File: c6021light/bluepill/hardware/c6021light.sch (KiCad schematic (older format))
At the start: 77 parts, among them J1 Barrel_Jack_Switch, J10 Conn_01x02, J11 Conn_01x02, J12 XpressNet, J2 Conn_02x04_Odd_Even, J3 Conn_02x16_Row_Letter_First, J30 Loconet, J31 Conn_01x02, J32 Conn_01x02, J4 Conn_01x02, J5 Grove I2C, J50 USB_B_Micro, J51 Conn_01x06, J52 Debug UART, J6 Conn_01x02, J7 Conn_01x02, J8 RJ45, Q30 BC337, Q31 BC547, Q32 BC547, SW1 SW_Push, U1 L7805, U10 SN75176, U2 L7808, U3 MCP2562, U30 LM393, U4 ISO1050DUB, U50 CH340C

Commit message: work on new revision
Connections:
- net +12V: no longer TP1.1 (Pin_1), TP2.1 (Pin_1)
- net GNDD: no longer J8.5
- no-connect marks 24 -> 28
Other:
- moved on the sheet: TP1, TP2
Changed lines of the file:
@@
 Sheet 1 1
 Title "C6021 Light"
-Date "2020-06-09"
-Rev "1.0"
+Date "2020-08-03"
+Rev "1.1"
 Comp "Damian Philipp / Gerhard Bertelsmann"
 Comment1 ""
@@
 	7725 900  7725 1000
 $Comp
-L Connector:RJ45 J8
-U 1 1 5EDB2E8F
-P 9575 1200
-F 0 "J8" H 9245 1204 50  0000 R CNN
-F 1 "RJ45" H 9245 1295 50  0000 R CNN
-F 2 "w_conn_pc:mebp8" V 9575 1225 50  0001 C CNN
-F 3 "~" V 9575 1225 50  0001 C CNN
-	1    9575 1200
-	-1   0    0    1
-$EndComp
-$Comp
 L Device:C C5
 U 1 1 5EDB8D27
@@
 Wire Wire Line
 	9175 1200 9025 1200
-Wire Wire Line
-	9175 1300 9025 1300
 Wire Wire Line
 	9175 1400 8925 1400
@@
 	8925 1400 8925 1000
 Wire Wire Line
-	9025 1300 9025 1900
-Wire Wire Line
 	8325 1500 9175 1500
-Wire Wire Line
-	9025 1300 9025 1200
-Connection ~ 9025 1300
 Wire Notes Line
 	6975 2025 11200 2025
@@
 	1150 1425 1200 1425
 Wire Wire Line
-	1200 1425 1200 2050
-Wire Wire Line
 	1200 2400 1500 2400
 Connection ~ 1200 1425
@@
 Connection ~ 5850 4225
 $Comp
-L Connector_Generic:Conn_01x01 TP1
-U 1 1 5EE1214D
-P 1000 2050
-F 0 "TP1" H 918 1917 50  0000 C CNN
-F 1 "Conn_01x01" H 918 1916 50  0001 C CNN
-F 2 "TestPoint:Test_Point_NA" H 1000 2050 50  0001 C CNN
-F 3 "~" H 1000 2050 50  0001 C CNN
-	1    1000 2050
-	-1   0    0    1
-$EndComp
-Connection ~ 1200 2050
-Wire Wire Line
-	1200 2050 1200 2300
-$Comp
 L Connector_Generic:Conn_01x01 TP2
 U 1 1 5EE12B1B
-P 1000 2300
-F 0 "TP2" H 918 2167 50  0000 C CNN
-F 1 "Conn_01x01" H 918 2166 50  0001 C CNN
-F 2 "TestPoint:Test_Point_NA" H 1000 2300 50  0001 C CNN
-F 3 "~" H 1000 2300 50  0001 C CNN
-	1    1000 2300
+P 775 2300
+F 0 "TP2" H 693 2167 50  0000 C CNN
+F 1 "Conn_01x01" H 693 2166 50  0001 C CNN
+F 2 "TestPoint:Test_Point_NA" H 775 2300 50  0001 C CNN
+F 3 "~" H 775 2300 50  0001 C CNN
+	1    775  2300
 	-1   0    0    1
 $EndComp
-Connection ~ 1200 2300
-Wire Wire Line
-	1200 2300 1200 2400
 $Comp
 L Connector_Generic:Conn_02x04_Odd_Even J2
@@
 	10375 4775 10375 5025
 Connection ~ 10375 5025
+$Comp
+L Connector:RJ45 J8
+U 1 1 5EDB2E8F
+P 9575 1200
+F 0 "J8" H 9245 1204 50  0000 R CNN
+F 1 "RJ45" H 9245 1295 50  0000 R CNN
+F 2 "w_conn_pc:mebp8" V 9575 1225 50  0001 C CNN
+F 3 "~" V 9575 1225 50  0001 C CNN
+	1    9575 1200
+	-1   0    0    1
+$EndComp
+Wire Wire Line
+	9025 1200 9025 1900
+NoConn ~ 9175 1300
+NoConn ~ 10250 8475
+$Comp
+L Connector_Generic:Conn_01x01 TP1
+U 1 1 5EE1214D
+P 775 2050
+F 0 "TP1" H 693 1917 50  0000 C CNN
+F 1 "Conn_01x01" H 693 1916 50  0001 C CNN
+F 2 "TestPoint:Test_Point_NA" H 775 2050 50  0001 C CNN
+F 3 "~" H 775 2050 50  0001 C CNN
+	1    775  2050
+	-1   0    0    1
+$EndComp
+NoConn ~ 975  2050
+Wire Wire Line
+	1200 1425 1200 2400
+NoConn ~ 975  2300
 $EndSCHEMATC

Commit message: fix some bugs on PCb
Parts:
- removed R50, R51: 0, Resistor_SMD:R_1206_3216Metric_Pad1.42x1.75mm_HandSolder, symbol Device:R
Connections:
- net CTS: now also J52.1 (Pin_1); no longer J52.5 (Pin_5)
- net DTR: no longer J52.1 (Pin_1)
- net GND: now also J50.6 (Shield)
- net RTS: now reaches J51.6 (Pin_6), U50.14 (~RTS)
- net RTS: now also J52.5 (Pin_5)
- net at C50.1, C51.1, U50.16 (VCC): now also J50.1 (VBUS)
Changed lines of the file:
@@
 Wire Wire Line
 	8175 5700 8175 5750
-$Comp
-L Device:R R50
-U 1 1 60480953
-P 4000 7200
-F 0 "R50" V 3900 7175 50  0000 L CNN
-F 1 "0" V 4000 7175 50  0000 L CNN
-F 2 "Resistor_SMD:R_1206_3216Metric_Pad1.42x1.75mm_HandSolder" V 3930 7200 50  0001 C CNN
-F 3 "~" H 4000 7200 50  0001 C CNN
-	1    4000 7200
-	1    0    0    -1
-$EndComp
 Wire Wire Line
 	4000 7350 4100 7350
@@
 Wire Wire Line
 	4100 7350 4100 7400
-Wire Wire Line
-	4000 7000 4000 7050
 $Comp
 L Device:C C51
@@
 Wire Wire Line
 	4625 5800 4625 5700
-Wire Wire Line
-	5300 5700 5300 5950
 Connection ~ 4625 5800
 Wire Wire Line
@@
 Wire Wire Line
 	5200 6100 5200 5800
-$Comp
-L Device:R R51
-U 1 1 6058F371
-P 4225 6000
-F 0 "R51" V 4125 5975 50  0000 L CNN
-F 1 "0" V 4225 5975 50  0000 L CNN
-F 2 "Resistor_SMD:R_1206_3216Metric_Pad1.42x1.75mm_HandSolder" V 4155 6000 50  0001 C CNN
-F 3 "~" H 4225 6000 50  0001 C CNN
-	1    4225 6000
-	1    0    0    -1
-$EndComp
-Wire Wire Line
-	4225 5850 4225 5700
 Wire Wire Line
 	4225 5700 4625 5700
@@
 Wire Wire Line
 	6475 6275 6275 6275
-Text Label 6275 6275 0    50   ~ 0
-DTR
 Wire Wire Line
 	6475 6675 6275 6675
-Text Label 6275 6675 0    50   ~ 0
-CTS
 NoConn ~ 6475 6575
 Wire Notes Line
@@
 Text Notes 8950 2400 0    50   ~ 0
 optional\ngalvanische Trennung CAN
-Wire Wire Line
-	4225 6150 4225 6175
 Wire Wire Line
 	4225 6175 4400 6175
@@
 	1    0    0    -1
 $EndComp
-$Comp
-L power:PWR_FLAG #FLG0103
-U 1 1 60D33B68
-P 5500 5875
-F 0 "#FLG0103" H 5500 5950 50  0001 C CNN
-F 1 "PWR_FLAG" H 5500 6048 50  0000 C CNN
-F 2 "" H 5500 5875 50  0001 C CNN
-F 3 "~" H 5500 5875 50  0001 C CNN
-	1    5500 5875
-	1    0    0    -1
-$EndComp
-Wire Wire Line
-	5300 5950 5500 5950
-Wire Wire Line
-	5500 5950 5500 5875
-Connection ~ 5300 5950
-Wire Wire Line
-	5300 5950 5300 6100
 $Comp
 L Connector_Generic:Conn_01x04 J5
@@
 	1200 1425 1200 2400
 NoConn ~ 975  2300
+Wire Wire Line
+	4000 7000 4000 7350
+Wire Wire Line
+	4225 5700 4225 6175
+Wire Wire Line
+	5300 5700 5300 6100
+Text Label 5750 7100 0    50   ~ 0
+RTS
+Text Label 6275 6675 0    50   ~ 0
+RTS
+Text Label 6275 6275 0    50   ~ 0
+CTS
 $EndSCHEMATC

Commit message: remove C32
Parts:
- removed C32: 1n, Capacitor_THT:C_Disc_D3.0mm_W1.6mm_P2.50mm, symbol Device:C
- J50: symbol Connector:USB_B_Micro -> c6021light-rescue:USB_B_Micro-Connector
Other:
- moved on the sheet: R40
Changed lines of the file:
@@
 Sheet 1 1
 Title "C6021 Light"
-Date "2020-08-03"
-Rev "1.1"
+Date "2020-12-16"
+Rev "1.2"
 Comp "Damian Philipp / Gerhard Bertelsmann"
 Comment1 ""
@@
 $EndComp
 $Comp
-L Connector:USB_B_Micro J50
+L c6021light-rescue:USB_B_Micro-Connector J50
 U 1 1 5F7EF982
 P 4100 6600
@@
 L Device:R R40
 U 1 1 6000FEAA
-P 8825 6200
-F 0 "R40" V 8750 6125 50  0000 L CNN
-F 1 "1k5" V 8825 6125 50  0000 L CNN
-F 2 "Resistor_THT:R_Axial_DIN0207_L6.3mm_D2.5mm_P7.62mm_Horizontal" V 8755 6200 50  0001 C CNN
-F 3 "~" H 8825 6200 50  0001 C CNN
-	1    8825 6200
+P 8825 6300
+F 0 "R40" V 8750 6225 50  0000 L CNN
+F 1 "1k5" V 8825 6225 50  0000 L CNN
+F 2 "Resistor_THT:R_Axial_DIN0207_L6.3mm_D2.5mm_P7.62mm_Horizontal" V 8755 6300 50  0001 C CNN
+F 3 "~" H 8825 6300 50  0001 C CNN
+	1    8825 6300
 	0    1    1    0
 $EndComp
@@
 	9075 6025 9025 6025
 Wire Wire Line
-	9025 6025 9025 6200
-Wire Wire Line
-	9025 6200 8975 6200
-$Comp
-L Device:C C32
-U 1 1 6008C60D
-P 8825 6400
-F 0 "C32" V 8750 6450 50  0000 L CNN
-F 1 "1n" V 8875 6475 50  0000 L CNN
-F 2 "Capacitor_THT:C_Disc_D3.0mm_W1.6mm_P2.50mm" H 8863 6250 50  0001 C CNN
-F 3 "~" H 8825 6400 50  0001 C CNN
-	1    8825 6400
-	0    1    1    0
-$EndComp
-Wire Wire Line
-	9025 6400 8975 6400
-Wire Wire Line
-	8675 6200 8675 6300
-Wire Wire Line
 	8675 6300 8425 6300
 Wire Wire Line
 	8425 6150 8400 6150
-Connection ~ 8675 6300
-Wire Wire Line
-	8675 6300 8675 6400
 Wire Wire Line
 	8425 5475 8425 5950
@@
 Wire Wire Line
 	8425 6300 8425 6150
-Connection ~ 9025 6200
-Wire Wire Line
-	9025 6200 9025 6400
 $Comp
 L power:GND #PWR0152
@@
 Text Label 6275 6275 0    50   ~ 0
 CTS
+Wire Wire Line
+	8975 6300 9025 6300
+Wire Wire Line
+	9025 6025 9025 6300
 $EndSCHEMATC

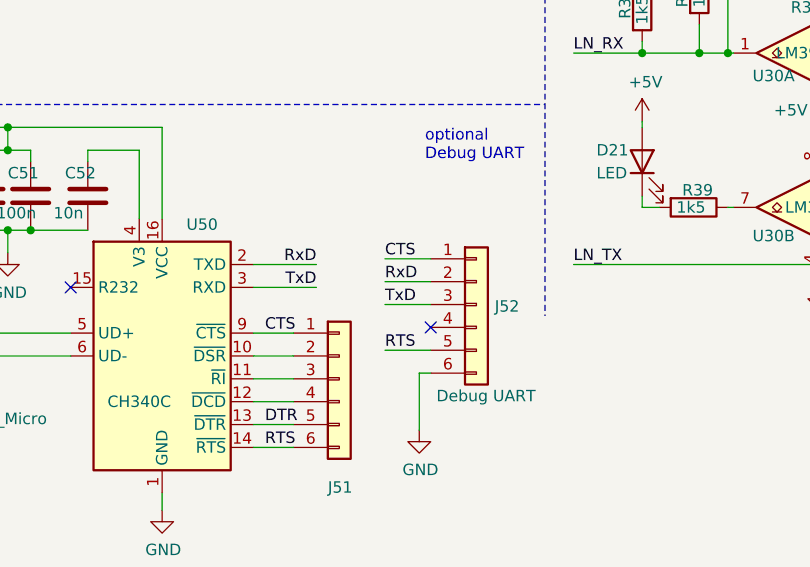
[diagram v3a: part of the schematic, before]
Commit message: swap TxD and RxD on J52 header for standard USB2Serial Moduls
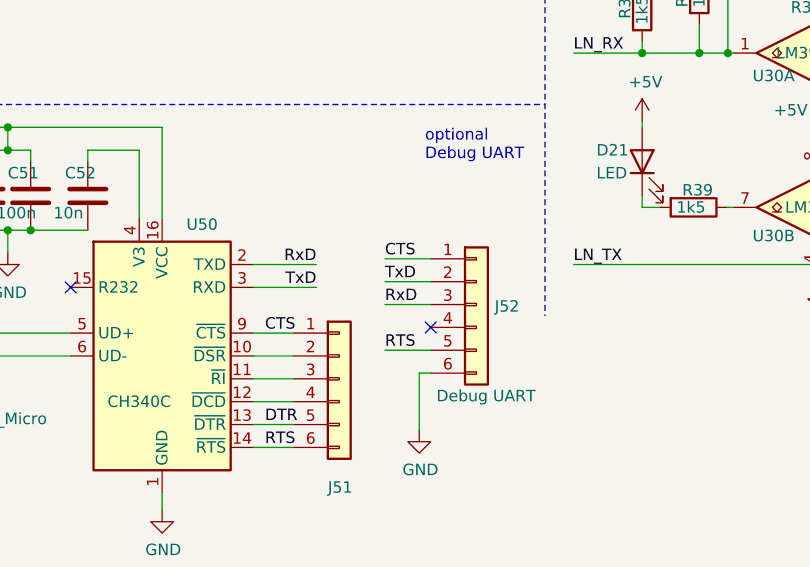
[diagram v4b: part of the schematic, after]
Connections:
- net RxD: now also J52.3 (Pin_3); no longer J52.2 (Pin_2)
- net TxD: now also J52.2 (Pin_2); no longer J52.3 (Pin_3)
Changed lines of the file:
@@
 Sheet 1 1
 Title "C6021 Light"
-Date "2020-12-16"
-Rev "1.2"
+Date "2021-01-08"
+Rev "1.3"
 Comp "Damian Philipp / Gerhard Bertelsmann"
 Comment1 ""
@@
 $EndComp
 Text Label 6275 6375 0    50   ~ 0
-RxD
+TxD
 Wire Wire Line
 	6475 6475 6275 6475
 Text Label 6275 6475 0    50   ~ 0
-TxD
+RxD
 Wire Wire Line
 	3800 3025 3625 3025

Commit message: wip
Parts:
- removed J31: Conn_01x02, Connector_PinHeader_2.54mm:PinHeader_1x02_P2.54mm_Vertical_NB, symbol Connector_Generic:Conn_01x02
- added J31: Conn_01x03, Connector_PinHeader_2.54mm:PinHeader_1x03_P2.54mm_Vertical, symbol Connector_Generic:Conn_01x03
- C30: footprint Capacitor_THT:C_Disc_D3.0mm_W1.6mm_P2.50mm -> Capacitor_THT:C_Rect_L7.0mm_W3.5mm_P2.50mm_P5.00mm
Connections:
- net +12V: now also J31.3 (Pin_3)
- net +8V: now also J31.1 (Pin_1)
- net at Q31.1 (C), R42.2: now also J31.2 (Pin_2)
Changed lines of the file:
@@
 Sheet 1 1
 Title "C6021 Light"
-Date "2021-01-08"
+Date "2021-03-03"
 Rev "1.3"
 Comp "Damian Philipp / Gerhard Bertelsmann"
@@
 F 0 "C30" H 9800 5550 50  0000 L CNN
 F 1 "47p" H 9800 5375 50  0000 L CNN
-F 2 "Capacitor_THT:C_Disc_D3.0mm_W1.6mm_P2.50mm" H 9813 5325 50  0001 C CNN
+F 2 "Capacitor_THT:C_Rect_L7.0mm_W3.5mm_P2.50mm_P5.00mm" H 9813 5325 50  0001 C CNN
 F 3 "~" H 9775 5475 50  0001 C CNN
 	1    9775 5475
@@
 L power:+12V #PWR0163
 U 1 1 5F098754
-P 10325 3225
-F 0 "#PWR0163" H 10325 3075 50  0001 C CNN
-F 1 "+12V" H 10340 3398 50  0000 C CNN
-F 2 "" H 10325 3225 50  0001 C CNN
-F 3 "" H 10325 3225 50  0001 C CNN
-	1    10325 3225
+P 10200 3225
+F 0 "#PWR0163" H 10200 3075 50  0001 C CNN
+F 1 "+12V" H 10175 3375 50  0000 C CNN
+F 2 "" H 10200 3225 50  0001 C CNN
+F 3 "" H 10200 3225 50  0001 C CNN
+	1    10200 3225
 	1    0    0    -1
 $EndComp
@@
 Wire Wire Line
 	10475 5225 10175 5225
-$Comp
-L Connector_Generic:Conn_01x02 J31
-U 1 1 5F0FF03F
-P 10125 3375
-F 0 "J31" H 10300 3475 50  0000 C CNN
-F 1 "Conn_01x02" H 10043 3141 50  0001 C CNN
-F 2 "Connector_PinHeader_2.54mm:PinHeader_1x02_P2.54mm_Vertical_NB" H 10125 3375 50  0001 C CNN
-F 3 "~" H 10125 3375 50  0001 C CNN
-	1    10125 3375
-	-1   0    0    1
-$EndComp
-Wire Wire Line
-	10450 3375 10325 3375
+Wire Wire Line
+	10450 3375 10200 3375
 Connection ~ 10450 3375
 Wire Wire Line
@@
 	10450 3275 10800 3275
 Wire Wire Line
-	10325 3225 10325 3275
+	10200 3225 10200 3275
 Wire Notes Line
 	6975 4375 9825 4375
@@
 Wire Wire Line
 	9025 6025 9025 6300
+$Comp
+L Connector_Generic:Conn_01x03 J31
+U 1 1 6061ABCD
+P 10000 3375
+F 0 "J31" H 10000 3175 50  0000 C CNN
+F 1 "Conn_01x03" H 9918 3141 50  0001 C CNN
+F 2 "Connector_PinHeader_2.54mm:PinHeader_1x03_P2.54mm_Vertical" H 10000 3375 50  0001 C CNN
+F 3 "~" H 10000 3375 50  0001 C CNN
+	1    10000 3375
+	-1   0    0    1
+$EndComp
+Wire Wire Line
+	10200 3475 10350 3475
+Wire Wire Line
+	10350 3475 10350 3225
+$Comp
+L power:+8V #PWR0165
+U 1 1 6069FF10
+P 10350 3225
+F 0 "#PWR0165" H 10350 3075 50  0001 C CNN
+F 1 "+8V" H 10375 3375 50  0000 C CNN
+F 2 "" H 10350 3225 50  0001 C CNN
+F 3 "" H 10350 3225 50  0001 C CNN
+	1    10350 3225
+	1    0    0    -1
+$EndComp
 $EndSCHEMATC
